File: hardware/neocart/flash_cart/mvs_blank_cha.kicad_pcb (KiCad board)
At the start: 2 copper layers, 174 x 134 mm, 120 parts

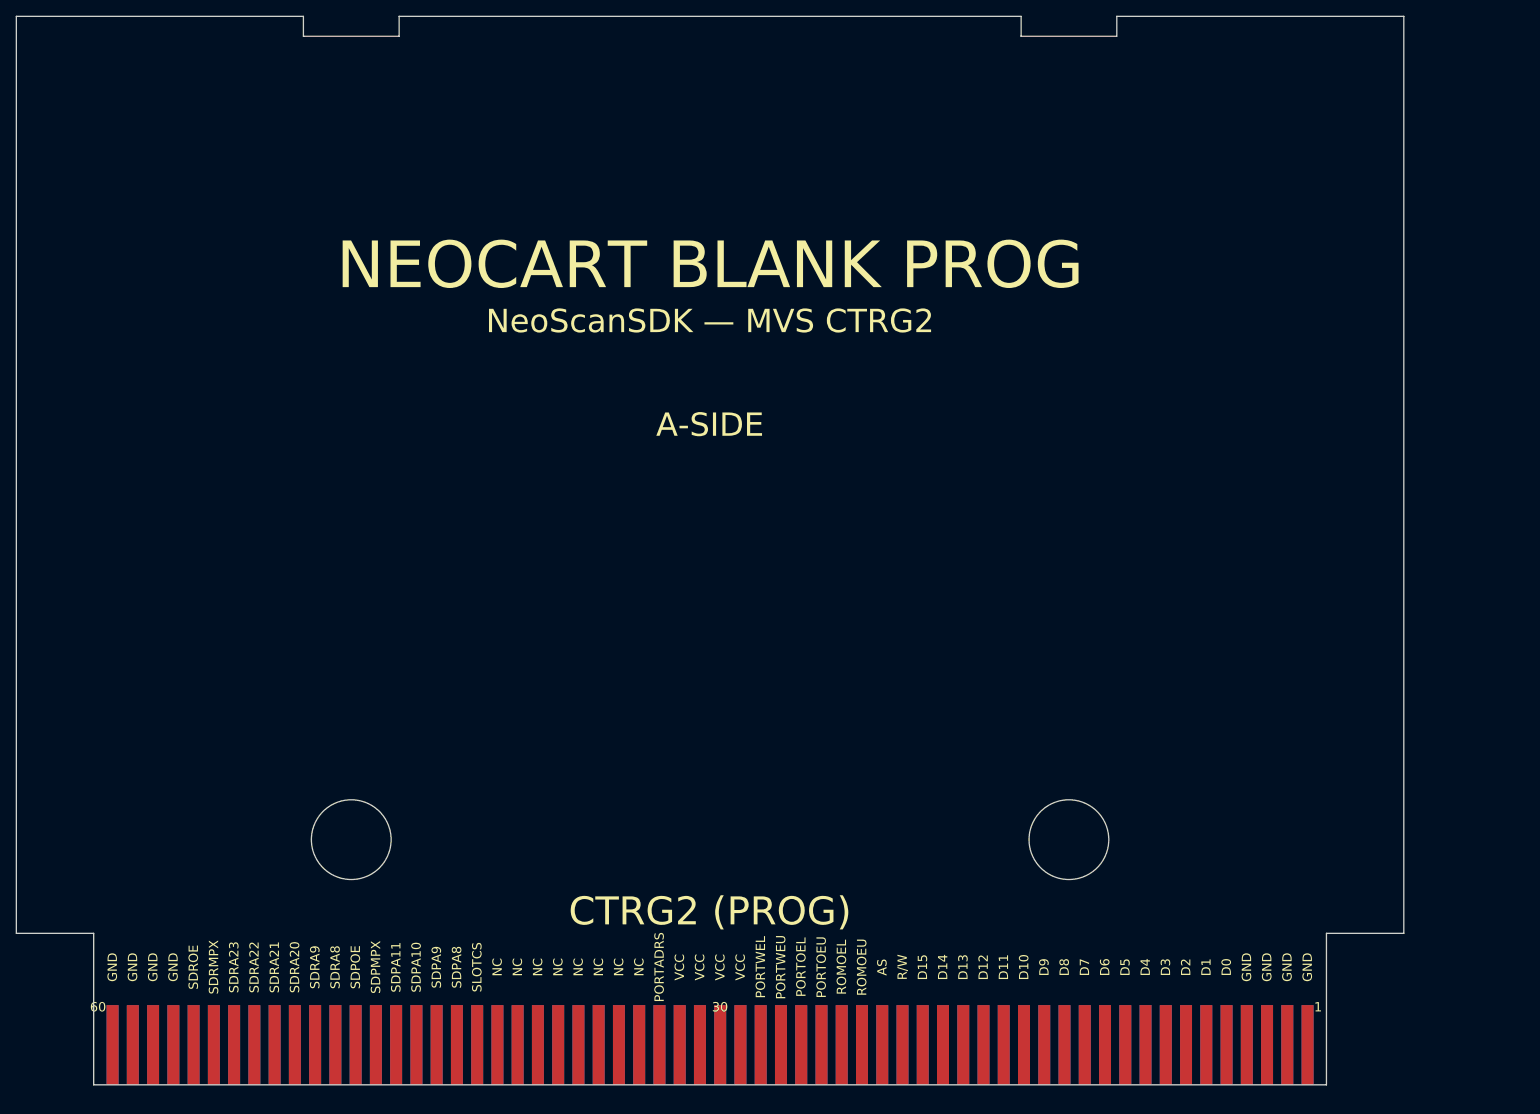
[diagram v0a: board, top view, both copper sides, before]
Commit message: Blank MVS boards: PROG (CTRG2) + CHA (CTRG1) with labeled pinouts
Two blank MVS cart PCBs built from scratch matching reference geometry:

PROG board (mvs_blank_prog.kicad_pcb):
- 174x134mm, notches, M5 mounting holes from neogeo-diag-mvs-prog
- 60 gold finger pads per side, full CTRG2 pinout
- F.SilkS: A-side labels, B.SilkS: B-side labels (1.17mm, 1 per pin)

CHA board (mvs_blank_cha.kicad_pcb):
- 174x134mm, notches, M5 mounting holes from neogeo-diag-mvs-cha
- 60 gold finger pads per side, full CTRG1 pinout
- F.SilkS: A-side labels, B.SilkS: B-side labels (1.17mm, 1 per pin)

Viewer: 4-panel live HTML at localhost:8042, auto-refresh 2.5s

Co-Authored-By: Claude Opus 4.6 (1M context) <noreply@anthropic.com>
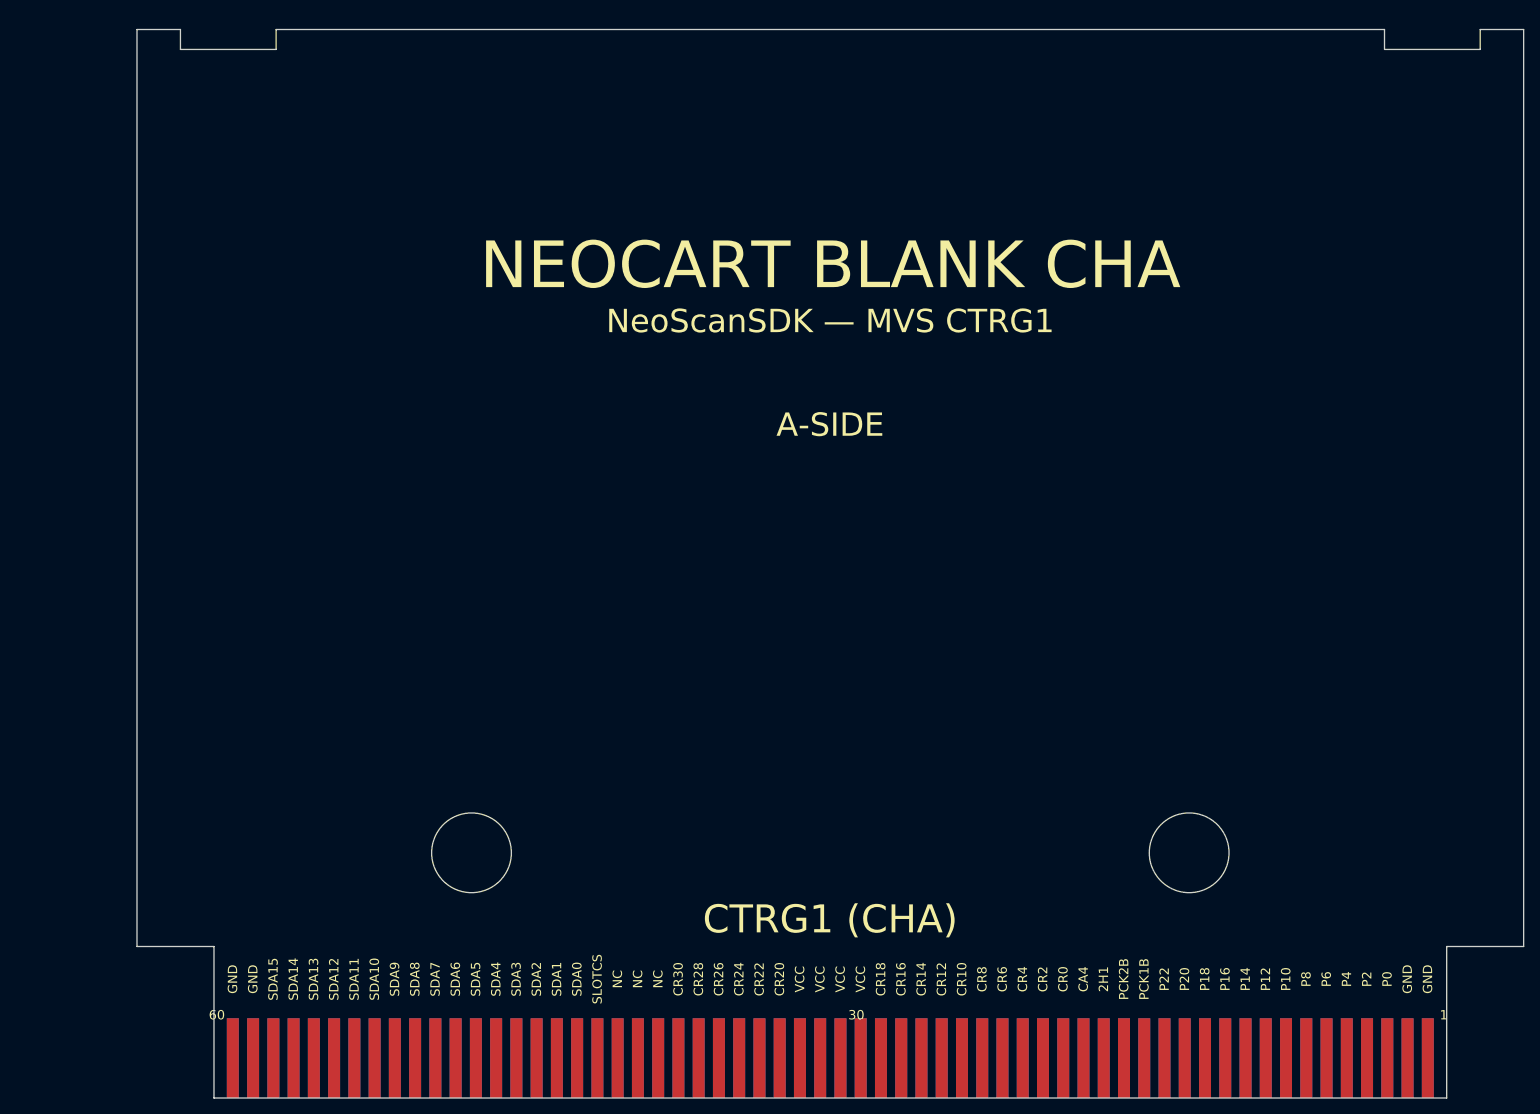
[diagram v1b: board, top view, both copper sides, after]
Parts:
- A10: value D5 -> P14
- A11: value D6 -> P16
- A12: value D7 -> P18
- A13: value D8 -> P20
- A14: value D9 -> P22
- A15: value D10 -> PCK1B
- A16: value D11 -> PCK2B
- A17: value D12 -> 2H1
- A18: value D13 -> CA4
- A19: value D14 -> CR0
- A20: value D15 -> CR2
- A21: value R/W -> CR4
- A22: value AS -> CR6
- A23: value ROMOEU -> CR8
- A24: value ROMOEL -> CR10
- A25: value PORTOEU -> CR12
- A26: value PORTOEL -> CR14
- A27: value PORTWEU -> CR16
- A28: value PORTWEL -> CR18
- A3: value GND -> P0
- A33: value PORTADRS -> CR20
- A34: value NC -> CR22
- A35: value NC -> CR24
- A36: value NC -> CR26
- A37: value NC -> CR28
- A38: value NC -> CR30
- A4: value GND -> P2
- A43: value SDPA8 -> SDA0
- A44: value SDPA9 -> SDA1
- A45: value SDPA10 -> SDA2
- A46: value SDPA11 -> SDA3
- A47: value SDPMPX -> SDA4
- A48: value SDPOE -> SDA5
- A49: value SDRA8 -> SDA6
- A5: value D0 -> P4
- A50: value SDRA9 -> SDA7
- A51: value SDRA20 -> SDA8
- A52: value SDRA21 -> SDA9
- A53: value SDRA22 -> SDA10
- A54: value SDRA23 -> SDA11
- A55: value SDRMPX -> SDA12
- A56: value SDROE -> SDA13
- A57: value GND -> SDA14
- A58: value GND -> SDA15
- A6: value D1 -> P6
- A7: value D2 -> P8
- A8: value D3 -> P10
- A9: value D4 -> P12
- B10: value A6 -> P15
- B11: value A7 -> P17
- B12: value A8 -> P19
- B13: value A9 -> P21
- B14: value A10 -> P23
- B15: value A11 -> 24M
- B16: value A12 -> 12M
- B17: value A13 -> 8M
- B18: value A14 -> RESET
- B19: value A15 -> CR1
- B20: value A16 -> CR3
- B21: value A17 -> CR5
- B22: value A18 -> CR7
- B23: value A19 -> CR9
- B24: value 68KCLKB -> CR11
- B25: value ROMWAIT -> CR13
- B26: value PWAIT0 -> CR15
- B27: value PWAIT1 -> CR17
- B28: value PDTACK -> CR19
- B3: value GND -> P1
- B33: value ROMOE -> CR21
- B34: value 4MB -> CR23
- B35: value RESET -> CR25
- B36: value NC -> CR27
- B37: value NC -> CR29
- B38: value NC -> CR31
- B39: value NC -> FIXD0
- B4: value GND -> P3
- B40: value NC -> FIXD1
- B41: value SDPAD0 -> FIXD2
- B42: value SDPAD1 -> FIXD3
- B43: value SDPAD2 -> FIXD4
- B44: value SDPAD3 -> FIXD5
- B45: value SDPAD4 -> FIXD6
- B46: value SDPAD5 -> FIXD7
- B47: value SDPAD6 -> SDRD0
- B48: value SDPAD7 -> SDRD1
- B49: value SDRAD0 -> SDROM
- B5: value A1 -> P5
- B50: value SDRAD1 -> SDMRD
- B51: value SDRAD2 -> SDD0
- B52: value SDRAD3 -> SDD1
- B53: value SDRAD4 -> SDD2
- B54: value SDRAD5 -> SDD3
- B55: value SDRAD6 -> SDD4
- B56: value SDRAD7 -> SDD5
- B57: value GND -> SDD6
- B58: value GND -> SDD7
- B6: value A2 -> P7
- B7: value A3 -> P9
- B8: value A4 -> P11
- B9: value A5 -> P13
- moved B60 164.9 mm to (229.8, 154.4)
- moved B59 159.9 mm to (227.2, 154.4)
- moved B58 154.8 mm to (224.7, 154.4)
- moved B57 149.7 mm to (222.1, 154.4)
- moved B56 144.6 mm to (219.6, 154.4)
- moved B55 139.5 mm to (217.1, 154.4)
- moved B1 134.8 mm to (79.9, 154.4)
- moved B54 134.5 mm to (214.5, 154.4)
- moved B2 129.7 mm to (82.4, 154.4)
- moved B53 129.4 mm to (212.0, 154.4)
- moved B3 124.6 mm to (85.0, 154.4)
- moved B52 124.3 mm to (209.4, 154.4)
- moved B4 119.6 mm to (87.5, 154.4)
- moved B51 119.2 mm to (206.9, 154.4)
- moved B5 114.5 mm to (90.1, 154.4)
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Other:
- board size 174 x 134 mm -> 173.9 x 134 mm
- board text added: "12M"
- board text added: "24M"
- board text added: "2H1"
- board text added: "8M"
- board text added: "CA4"
- board text added: "CR0"
- board text added: "CR1"
- board text added: "CR10"
- board text added: "CR11"
- board text added: "CR12"
- board text added: "CR13"
- board text added: "CR14"
- board text added: "CR15"
- board text added: "CR16"
- board text added: "CR17"
- board text added: "CR18"
- board text added: "CR19"
- board text added: "CR2"
- board text added: "CR20"
- board text added: "CR21"
- board text added: "CR22"
- board text added: "CR23"
- board text added: "CR24"
- board text added: "CR25"
- board text added: "CR26"
- board text added: "CR27"
- board text added: "CR28"
- board text added: "CR29"
- board text added: "CR3"
- board text added: "CR30"
- board text added: "CR31"
- board text added: "CR4"
- board text added: "CR5"
- board text added: "CR6"
- board text added: "CR7"
- board text added: "CR8"
- board text added: "CR9"
- board text added: "CTRG1 (CHA)"
- board text added: "FIXD0"
- board text added: "FIXD1"
- board text added: "FIXD2"
- board text added: "FIXD3"
- board text added: "FIXD4"
- board text added: "FIXD5"
- board text added: "FIXD6"
- board text added: "FIXD7"
- board text added: "NEOCART BLANK CHA"
- board text added: "NeoScanSDK — MVS CTRG1"
- board text added: "P0"
- board text added: "P1"
- board text added: "P10"
- board text added: "P11"
- board text added: "P12"
- board text added: "P13"
- board text added: "P14"
- board text added: "P15"
- board text added: "P16"
- board text added: "P17"
- board text added: "P18"
- board text added: "P19"
- board text added: "P2"
- board text added: "P20"
- board text added: "P21"
- board text added: "P22"
- board text added: "P23"
- board text added: "P3"
- board text added: "P4"
- board text added: "P5"
- board text added: "P6"
- board text added: "P7"
- board text added: "P8"
- board text added: "P9"
- board text added: "PCK1B"
- board text added: "PCK2B"
- board text added: "SDA0"
- board text added: "SDA1"
- board text added: "SDA10"
- board text added: "SDA11"
- board text added: "SDA12"
- board text added: "SDA13"
- board text added: "SDA14"
- board text added: "SDA15"
- board text added: "SDA2"
- board text added: "SDA3"
- board text added: "SDA4"
- board text added: "SDA5"
- board text added: "SDA6"
- board text added: "SDA7"
- board text added: "SDA8"
- board text added: "SDA9"
- board text added: "SDD0"
- board text added: "SDD1"
- board text added: "SDD2"
- board text added: "SDD3"
- board text added: "SDD4"
- board text added: "SDD5"
- board text added: "SDD6"
- board text added: "SDD7"
- board text added: "SDMRD"
- board text added: "SDRD0"
- board text added: "SDRD1"
- board text added: "SDROM"
- board text removed: "4MB"
- board text removed: "68KCLKB"
- board text removed: "A1"
- board text removed: "A10"
- board text removed: "A11"
- board text removed: "A12"
- board text removed: "A13"
- board text removed: "A14"
- board text removed: "A15"
- board text removed: "A16"
- board text removed: "A17"
- board text removed: "A18"
- board text removed: "A19"
- board text removed: "A2"
- board text removed: "A3"
- board text removed: "A4"
- board text removed: "A5"
- board text removed: "A6"
- board text removed: "A7"
- board text removed: "A8"
- board text removed: "A9"
- board text removed: "AS"
- board text removed: "CTRG2 (PROG)"
- board text removed: "D0"
- board text removed: "D1"
- board text removed: "D10"
- board text removed: "D11"
- board text removed: "D12"
- board text removed: "D13"
- board text removed: "D14"
- board text removed: "D15"
- board text removed: "D2"
- board text removed: "D3"
- board text removed: "D4"
- board text removed: "D5"
- board text removed: "D6"
- board text removed: "D7"
- board text removed: "D8"
- board text removed: "D9"
- board text removed: "NEOCART BLANK PROG"
- board text removed: "NeoScanSDK — MVS CTRG2"
- board text removed: "PDTACK"
- board text removed: "PORTADRS"
- board text removed: "PORTOEL"
- board text removed: "PORTOEU"
- board text removed: "PORTWEL"
- board text removed: "PORTWEU"
- board text removed: "PWAIT0"
- board text removed: "PWAIT1"
- board text removed: "R/W"
- board text removed: "ROMOE"
- board text removed: "ROMOEL"
- board text removed: "ROMOEU"
- board text removed: "ROMWAIT"
- board text removed: "SDPA10"
- board text removed: "SDPA11"
- board text removed: "SDPA8"
- board text removed: "SDPA9"
- board text removed: "SDPAD0"
- board text removed: "SDPAD1"
- board text removed: "SDPAD2"
- board text removed: "SDPAD3"
- board text removed: "SDPAD4"
- board text removed: "SDPAD5"
- board text removed: "SDPAD6"
- board text removed: "SDPAD7"
- board text removed: "SDPMPX"
- board text removed: "SDPOE"
- board text removed: "SDRA20"
- board text removed: "SDRA21"
- board text removed: "SDRA22"
- board text removed: "SDRA23"
- board text removed: "SDRA8"
- board text removed: "SDRA9"
- board text removed: "SDRAD0"
- board text removed: "SDRAD1"
- board text removed: "SDRAD2"
- board text removed: "SDRAD3"
- board text removed: "SDRAD4"
- board text removed: "SDRAD5"
- board text removed: "SDRAD6"
- board text removed: "SDRAD7"
- board text removed: "SDRMPX"
- board text removed: "SDROE"

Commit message: Remove orphan pin number markers (1, 30, 60) from both boards
Co-Authored-By: Claude Opus 4.6 (1M context) <noreply@anthropic.com>
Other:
- board text removed: "1"
- board text removed: "30"
- board text removed: "60"
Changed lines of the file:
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@@
 		(layer "Edge.Cuts")
-	)
-	(gr_text "60"
-		(at 77.9 149 0)
-		(layer "F.SilkS")
-		(effects
-			(font
-				(size 1.17 1.17)
-				(thickness 0.15)
-			)
-		)
-	)
-	(gr_text "30"
-		(at 158.1 149 0)
-		(layer "F.SilkS")
-		(effects
-			(font
-				(size 1.17 1.17)
-				(thickness 0.15)
-			)
-		)
-	)
-	(gr_text "1"
-		(at 231.76 149 0)
-		(layer "F.SilkS")
-		(effects
-			(font
-				(size 1.17 1.17)
-				(thickness 0.15)
-			)
-		)
 	)
 	(gr_text "GND"
